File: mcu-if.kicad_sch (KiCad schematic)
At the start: 9 parts

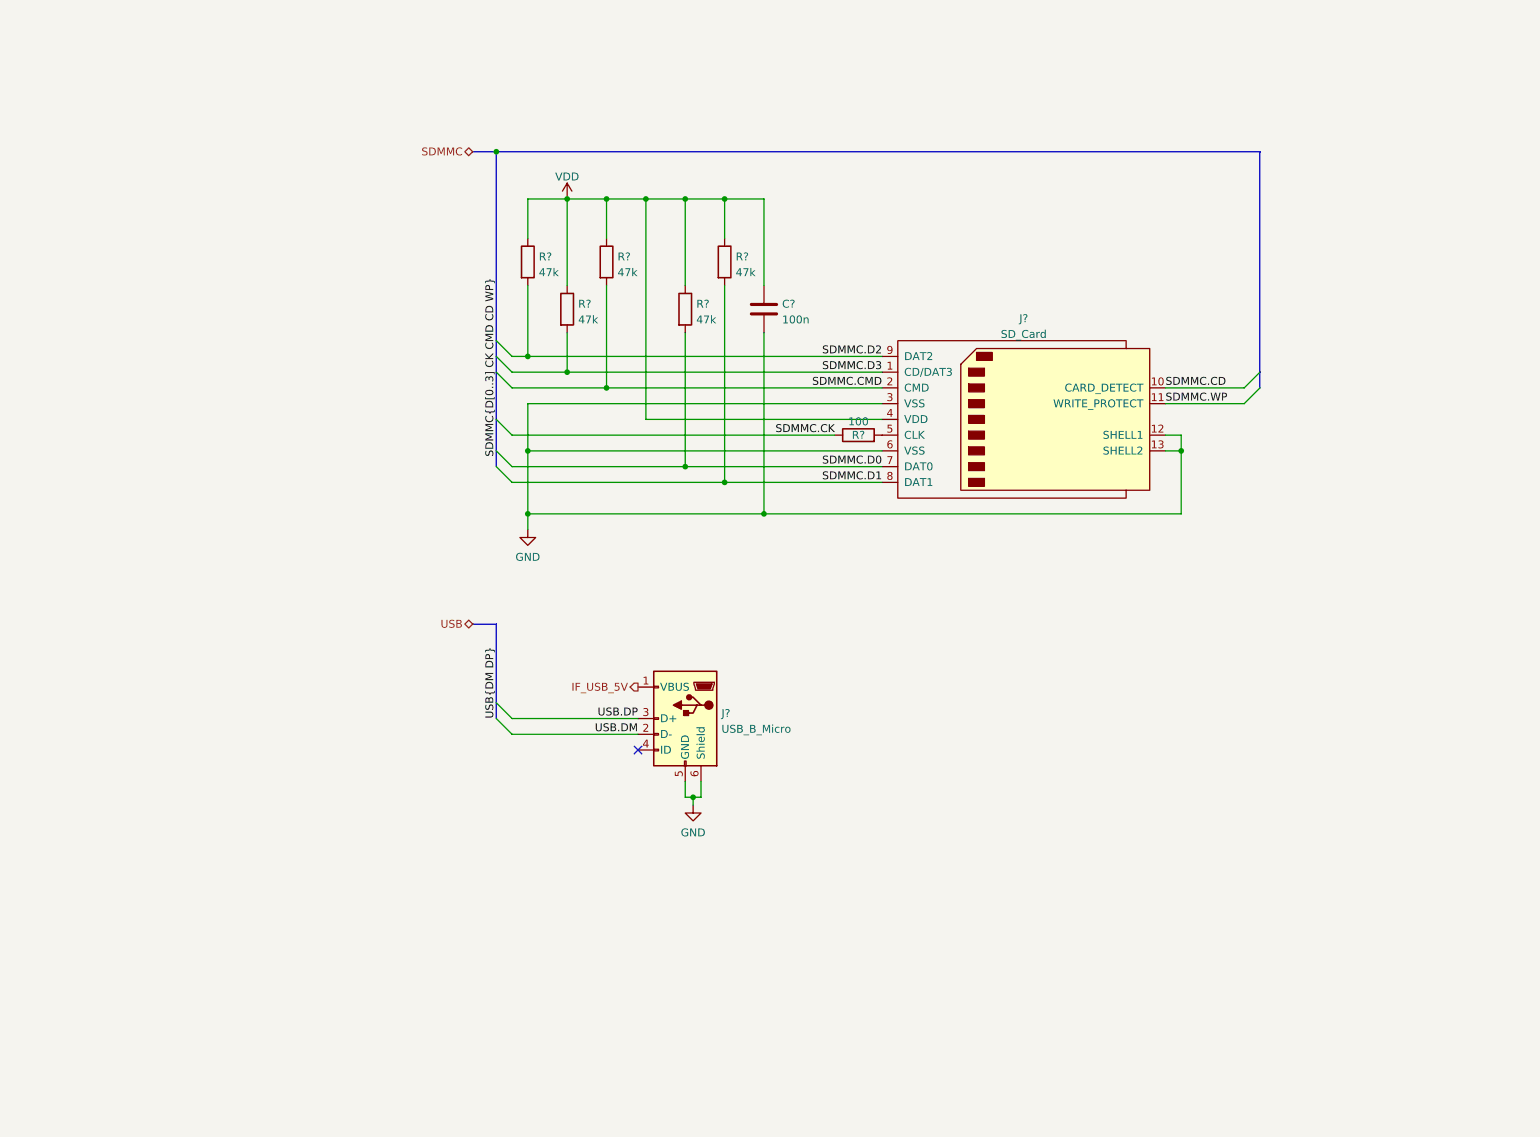
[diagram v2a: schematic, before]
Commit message: Add Ethernet interface.
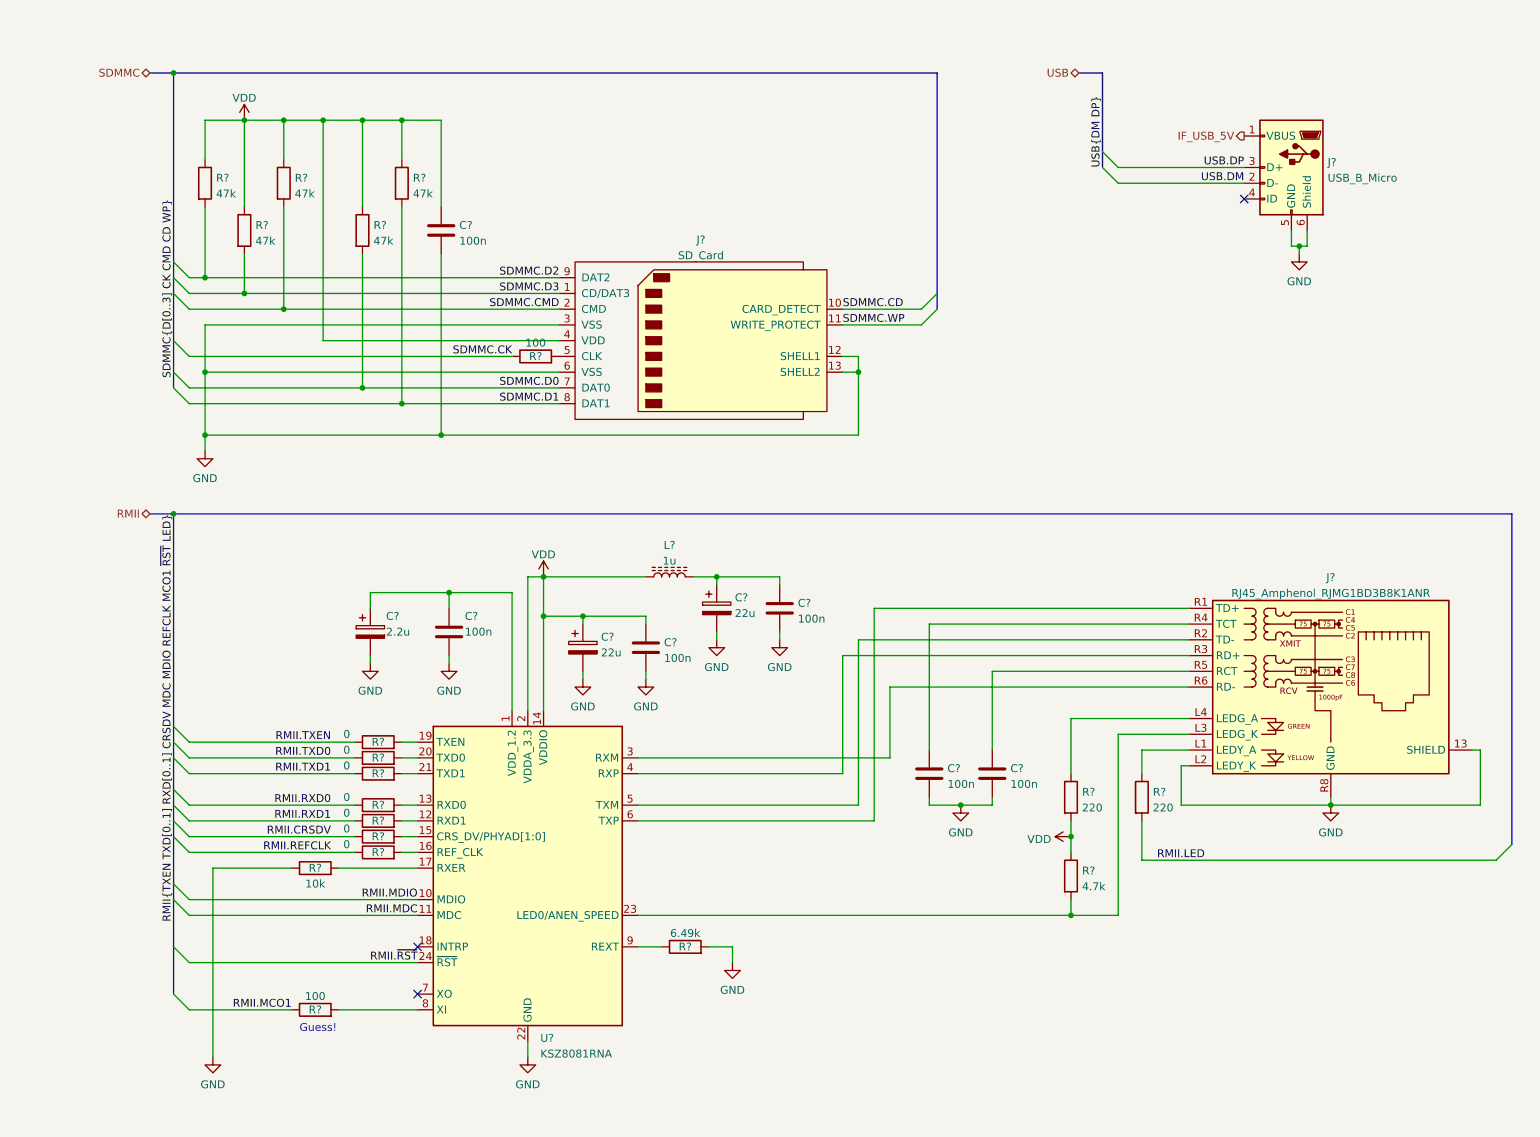
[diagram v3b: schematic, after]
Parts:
- added C? (x5): 100n, symbol Device:C
- added C? (x2): 22u, symbol Device:C_Polarized
- added C?: 2.2u, symbol Device:C_Polarized
- added J?: RJ45_Amphenol_RJMG1BD3B8K1ANR, Connector_RJ:RJ45_Amphenol_RJMG1BD3B8K1ANR, symbol Connector:RJ45_Amphenol_RJMG1BD3B8K1ANR
- added L?: 1u, symbol Device:L_Ferrite
- added R? (x7): 0, symbol Device:R
- added R?: 10k, symbol Device:R
- added R?: 6.49k, symbol Device:R
- added R? (x2): 220, symbol Device:R
- added R?: 100, symbol Device:R
- added R?: 4.7k, symbol Device:R
- added U?: KSZ8081RNA, Package_DFN_QFN:QFN-24-1EP_4x4mm_P0.5mm_EP2.6x2.6mm, symbol Interface_Ethernet:KSZ8081RNA
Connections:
- net GND: now also C?.2, C?.2, C?.2, C?.2, C?.2, C?.2, C?.2, C?.2, J?.13 (SHIELD), J?.L2 (LEDY_K), J?.R8 (GND), R?.1, R?.2, U?.22 (GND), U?.25 (GND)
- net VDD: now also C?.1, C?.1, L?.1, R?.1, R?.2, U?.14 (VDDIO), U?.2 (VDDA_3.3)
- new net: R?.2, U?.19 (TXEN)
- new net: R?.2, U?.16 (REF_CLK)
- new net: C?.1, J?.R4 (TCT)
- new net: C?.1, C?.1, L?.2
- new net: C?.1, C?.1, U?.1 (VDD_1.2)
- new net: J?.L1 (LEDY_A), R?.1
- new net: J?.L3 (LEDG_K), R?.2, U?.23 (LED0/ANEN_SPEED)
- new net: J?.L4 (LEDG_A), R?.1
- new net: J?.R1 (TD+), U?.6 (TXP)
- new net: J?.R2 (TD-), U?.5 (TXM)
- new net: J?.R3 (RD+), U?.4 (RXP)
- new net: C?.1, J?.R5 (RCT)
- new net: J?.R6 (RD-), U?.3 (RXM)
- new net: R?.2, U?.17 (RXER)
- new net: R?.2, U?.21 (TXD1)
- new net: R?.2, U?.12 (RXD1)
- new net: R?.1, U?.9 (REXT)
- new net: R?.2, U?.8 (XI)
- new net: R?.2, U?.13 (RXD0)
- new net: R?.2, U?.15 (CRS_DV/PHYAD[1:0])
- new net: R?.2, U?.20 (TXD0)
- new net RMII.CRSDV: R?.1
- new net RMII.LED: R?.2
- new net RMII.MCO1: R?.1
- new net RMII.MDC: U?.11 (MDC)
- new net RMII.MDIO: U?.10 (MDIO)
- new net RMII.REFCLK: R?.1
- new net RMII.RXD0: R?.1
- new net RMII.RXD1: R?.1
- new net RMII.TXD0: R?.1
- new net RMII.TXD1: R?.1
- new net RMII.TXEN: R?.1
- new net RMII.~{RST}: U?.24 (~{RST})
- no-connect marks 1 -> 3
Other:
- note added: "Guess!"
- moved on the sheet: C?, J?, R?

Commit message: Capacitor part assignment
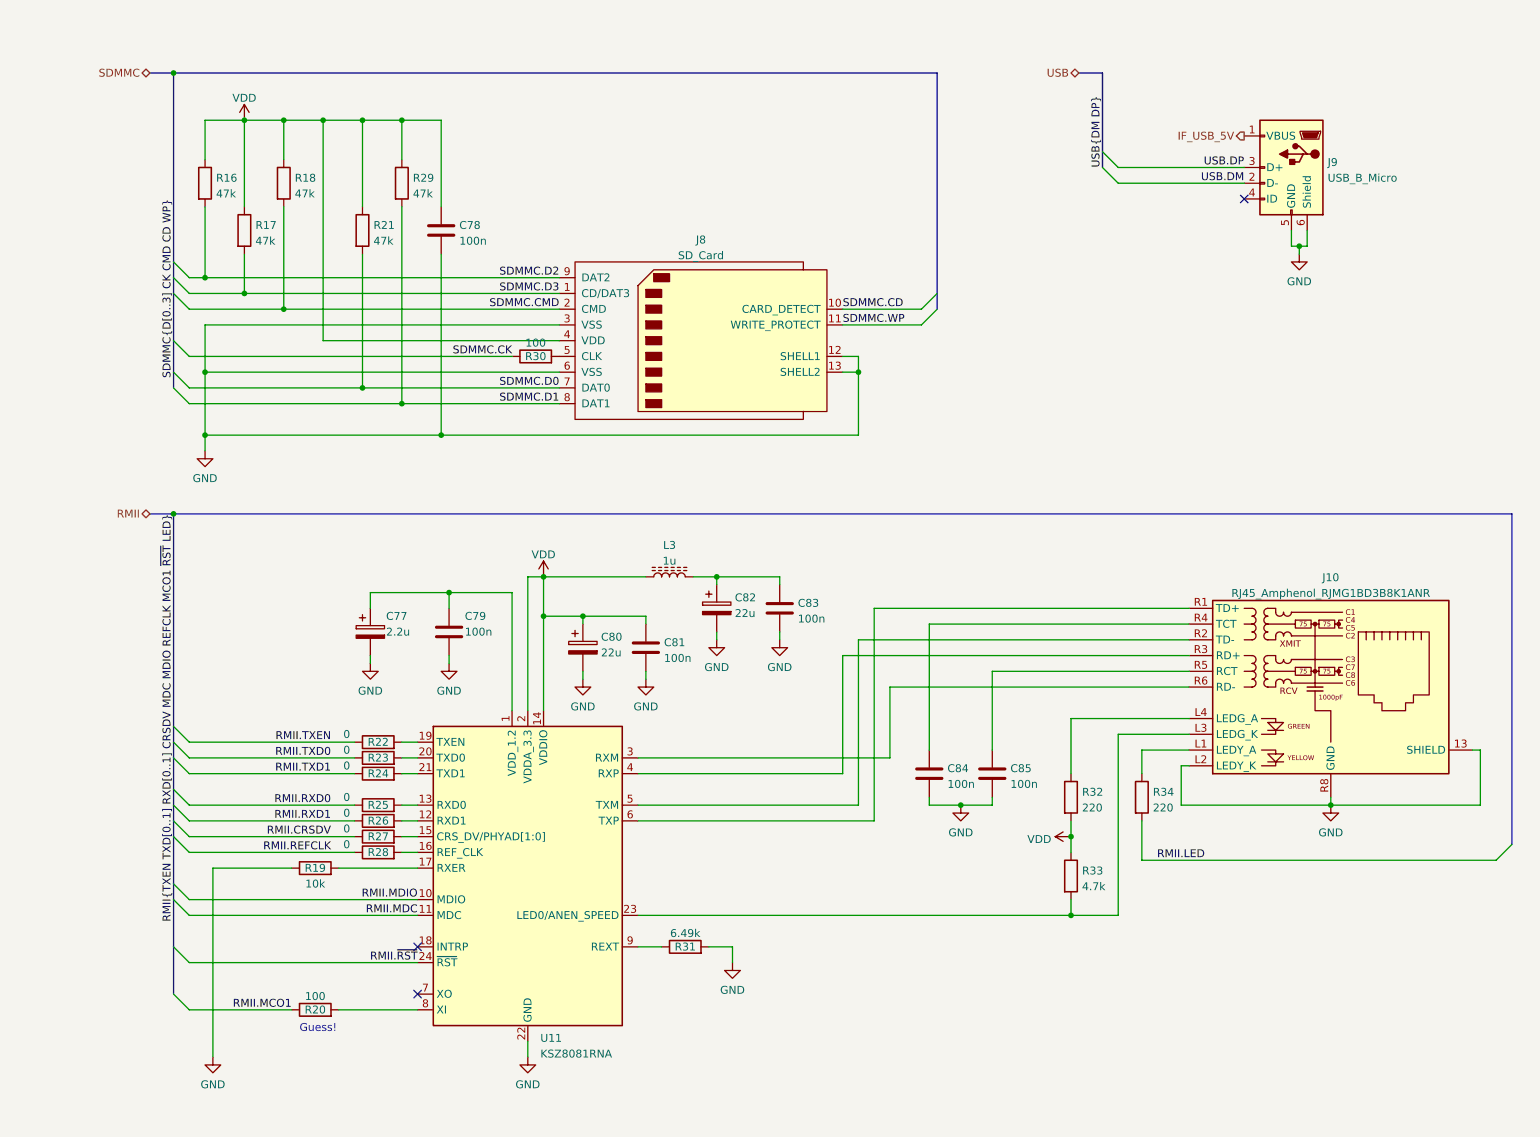
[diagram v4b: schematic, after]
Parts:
- C77: renamed from C?; footprint (none) -> Capacitor_SMD:C_0805_2012Metric_Pad1.18x1.45mm_HandSolder
- C79, C81, C83, C84, C85: renamed from C?; footprint (none) -> Capacitor_SMD:C_0603_1608Metric_Pad1.08x0.95mm_HandSolder
- C80, C82: renamed from C?; footprint (none) -> Capacitor_Tantalum_SMD:CP_EIA-3216-18_Kemet-A_Pad1.58x1.35mm_HandSolder; Part (none) -> 74-293D226X96R3A2TE3
- gave numbers to parts that had none: 25

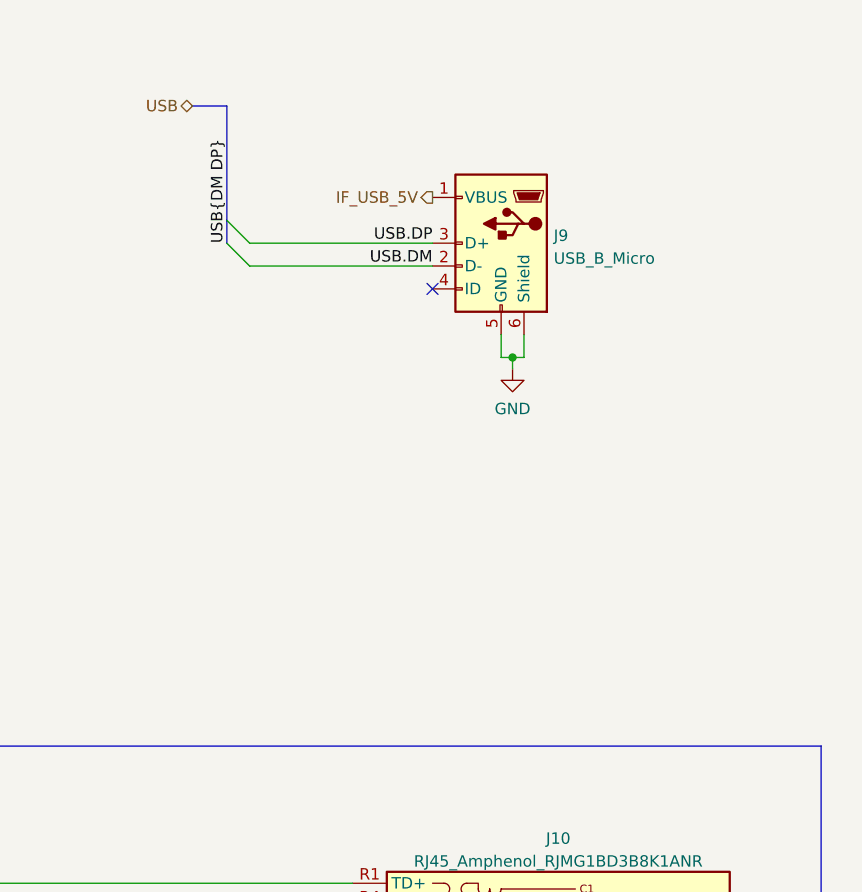
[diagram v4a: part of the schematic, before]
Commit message: Add display connector
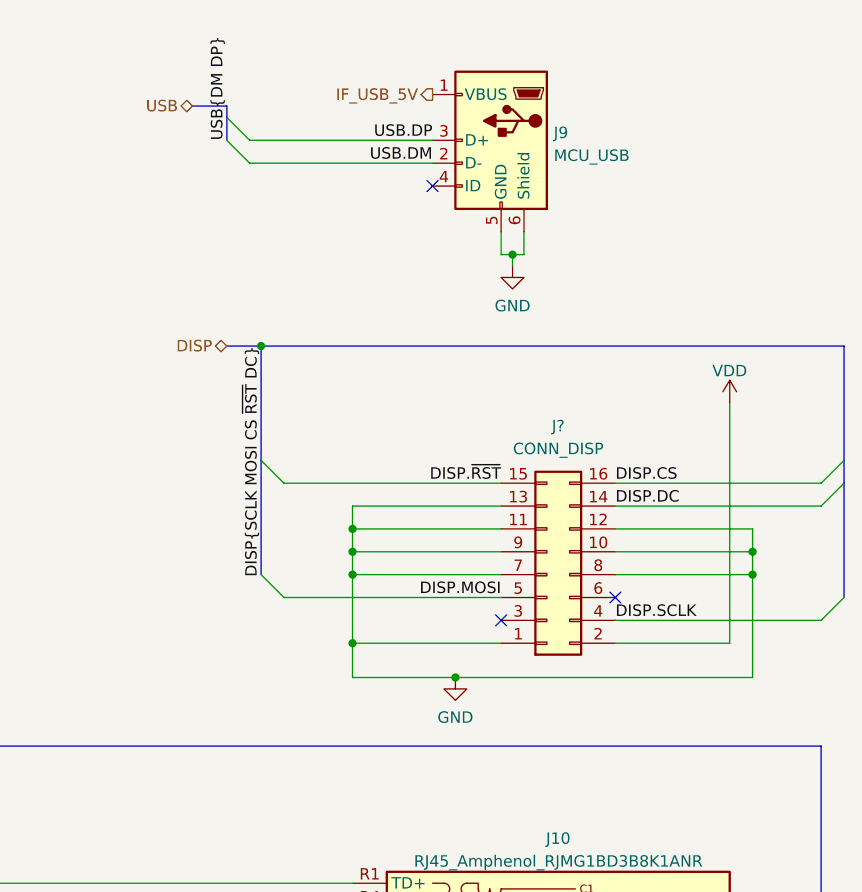
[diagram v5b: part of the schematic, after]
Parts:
- added J?: CONN_DISP, Connector_PinSocket_2.54mm:PinSocket_2x08_P2.54mm_Vertical, symbol Connector_Generic:Conn_02x08_Odd_Even
- J9: value USB_B_Micro -> MCU_USB
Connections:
- net GND: now also J?.1 (Pin_1), J?.10 (Pin_10), J?.11 (Pin_11), J?.12 (Pin_12), J?.13 (Pin_13), J?.7 (Pin_7), J?.8 (Pin_8), J?.9 (Pin_9)
- net VDD: now also J?.2 (Pin_2)
- new net DISP.CS: J?.16 (Pin_16)
- new net DISP.DC: J?.14 (Pin_14)
- new net DISP.MOSI: J?.5 (Pin_5)
- new net DISP.SCLK: J?.4 (Pin_4)
- new net DISP.~{RST}: J?.15 (Pin_15)
- no-connect marks 3 -> 5
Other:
- moved on the sheet: J9
